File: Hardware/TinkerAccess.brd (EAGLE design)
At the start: 65 x 56.5 mm, 46 parts, among them Q1 500mA/300V, Q2 310mA/60V/1.6Ω, U1 SOIC-8SOIC-8

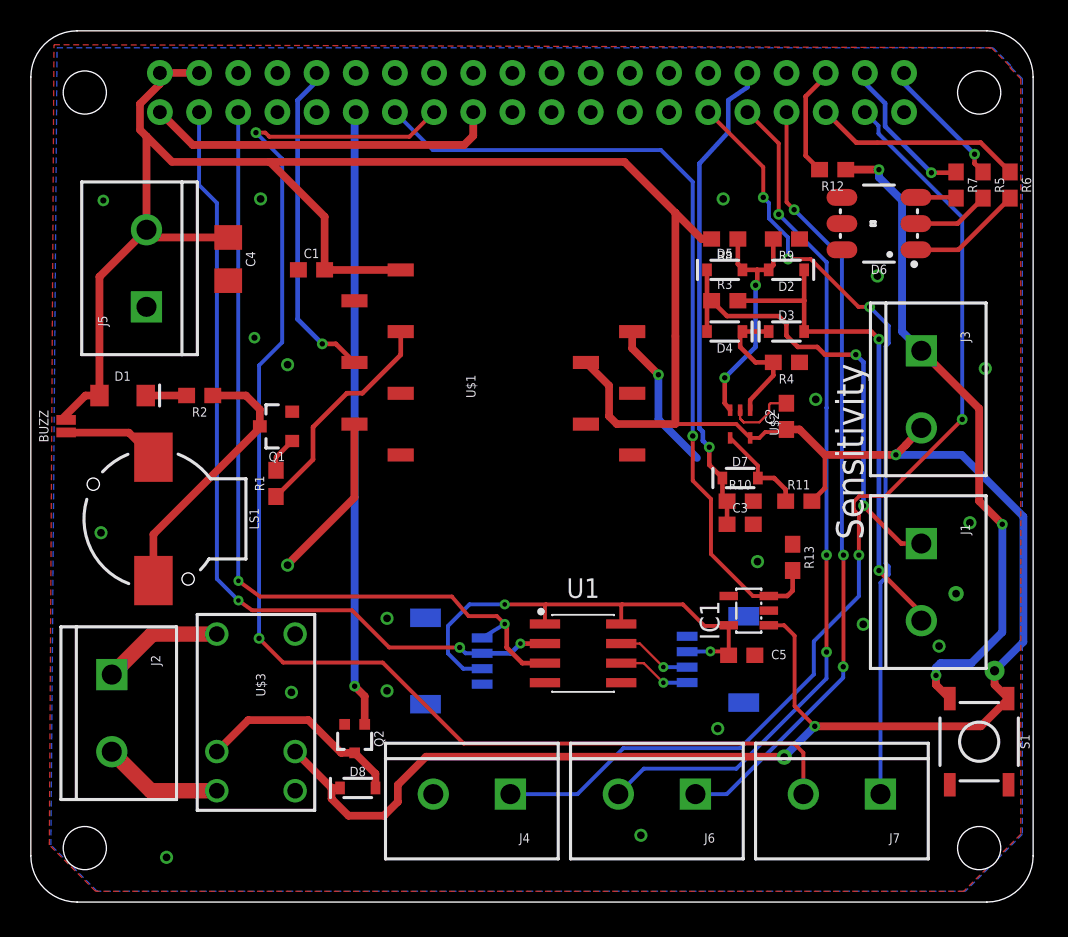
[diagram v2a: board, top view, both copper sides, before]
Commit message: Changes for v1.4 of TinkerAccess PCB
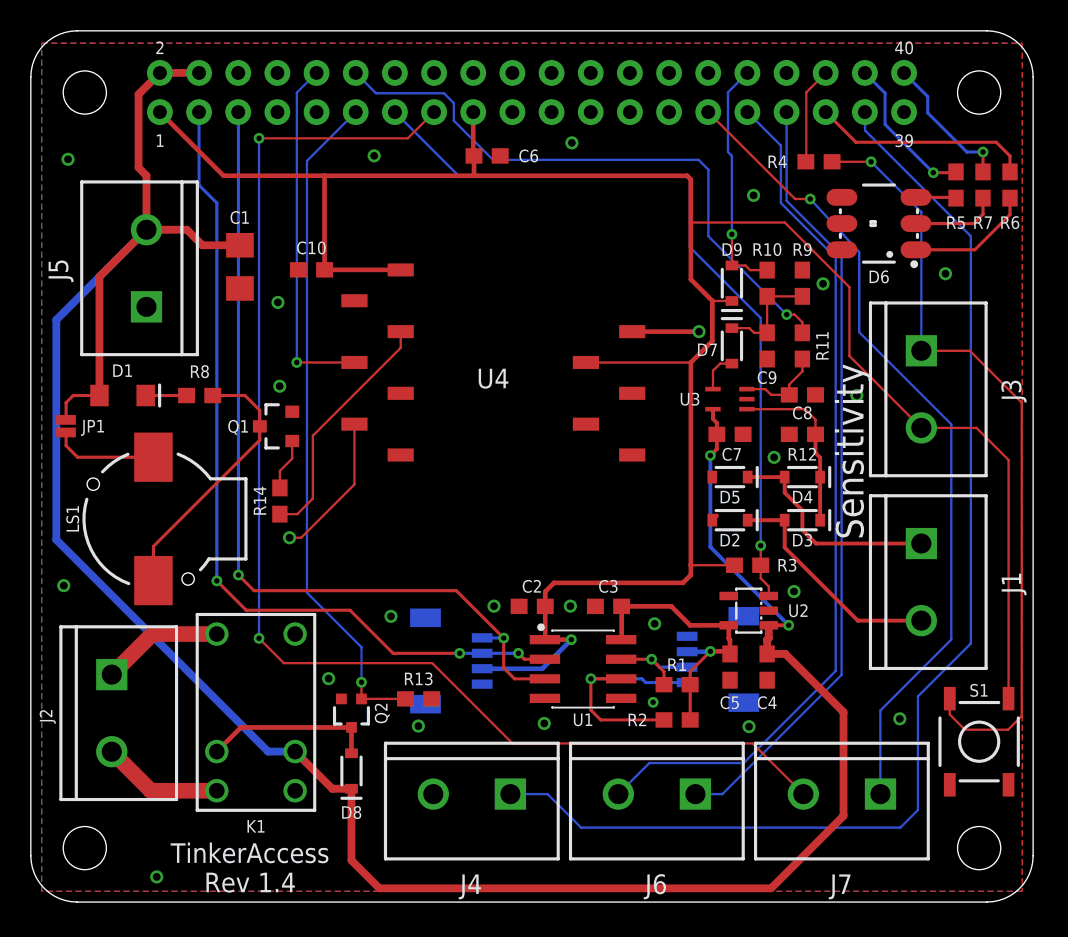
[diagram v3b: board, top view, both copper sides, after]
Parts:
- removed U$2: ADCMP-371, TinkerMill:SC-70-5
- added C10, C7: 0.1uF, SparkFun-Capacitors:0603
- added C6, C8, C9: 1uF, SparkFun-Capacitors:0603
- added D9: 1A/100V, SparkFun-DiscreteSemi:SOD-323
- added LOGO1: MADE_BY_TINKERMILL, TinkerMill:MADE_BY_TINKERMILL
- added R14: 180, SparkFun-Resistors:0603
- added U3: ADCMP-371, TinkerMill:SC-70-5
- C1: value 0.1uF -> 10uF; device SparkFun-Capacitors:0603 -> SparkFun-Capacitors:1206
- C2, C3: value 10uF -> 0.1uF
- C4: value 10uF -> 1uF; device SparkFun-Capacitors:1206 -> SparkFun-Capacitors:0603
- C5: value 10uF -> 1uF
- D2, D3, D4, D5, D7: value 250mA/100V -> 1A/100V
- D8: value 1A/23V/620mV -> 1A/100V
- JP1: value JUMPER-SMT_2_NC_PASTE_NO-SILK -> BUZZ
- LS1: value BUZZER-SMD -> BUZZER
- R1, R2: value 10M -> 10k
- R12: value 10k -> 1k
- R3, R4: value 1k -> 10k
- R5: value 330 -> 300
- R7: value 300 -> 330
- R8: value 1k -> 330
- R9: value 1k -> 100k
- U1: value SOIC-8SOIC-8 -> Si8600AC
- U2: value (none) -> AP2112
- moved C4 43.8 mm to (47.8, 15.2)
- moved R2 37.4 mm to (41.9, 11.8)
- moved R8 35.5 mm to (10.9, 32.9)
- moved R1 29.1 mm to (41.9, 14.1), turned to 180 degrees
- moved R13 25.9 mm to (25.1, 13.2), turned to 0 degrees
- moved C2 20.6 mm to (32.5, 19.2), turned to 0 degrees
- moved R12 17.3 mm to (50.0, 30.3), turned to 0 degrees
- moved R3 17.2 mm to (46.5, 21.8)
- moved D2 16.6 mm to (45.3, 24.8)
- moved R10 14.2 mm to (47.8, 40.1), turned to 90 degrees
- moved D5 13.4 mm to (45.3, 27.6), turned to 180 degrees
- moved R4 13.2 mm to (51.1, 48.0)
- moved D3 12.3 mm to (50.0, 24.8), turned to 180 degrees
- moved D4 10.7 mm to (50.0, 27.6)
- moved R11 10.1 mm to (50.0, 36.1), turned to 270 degrees
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- renumbered BUZZ to JP1, IC1 to U2, U$1 to U4, U$3 to K1
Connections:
- removed net N$8: U1.5
- removed net RECT-: D2.A, D5.A, R8.1, R9.2, U$2.P$3
- new net DETECT: C9.1, D7.C, R10.1, R9.1
- new net VREF: C8.1, R11.2, U3.3
- net +3V3: now also C3.2, R1.1, R2.1; no longer J8.2, U1.1
- net 3.3V: now also C10.2, C2.2, C6.1, D9.C, J3.2, J8.2, R3.1, S1.1, U1.1, U4.11, U4.2
- net 3.3V_EN: now also R3.2; no longer R13.2
- net 5V: now also C1.1, C7.1, U3.5; no longer C1.2, C2.1, J3.2, R11.2, R8.2, S1.1, U$2.P$5, U4.11, U4.2
- net AC1: no longer R3.1
- net AC2: no longer R3.2
- net BSCL: now also R2.2
- net BSDA: now also R1.2
- net COMPOUT: now also U3.4; no longer R11.1, U$2.P$4
- net GND: now also C1.2, C10.1, C2.1, C3.1, C6.2, C7.2, C8.2, C9.2, D2.A, D5.A, R12.1, R13.2, R9.2, U1.5, U3.2; no longer C1.1, C2.2, C3.2, R10.2, R13.1, R4.1, R9.1, U$2.P$2
- net GPIO12: now also D9.A, R10.2; no longer C3.1, D7.C, R10.1
- net GPIO16: now also R4.2; no longer R12.2
- net GPIO18: now also R11.1
- net LED_BLUE: now also R5.1; no longer R7.1
- net LED_RED: now also R7.1; no longer R5.1
- net LED_RFID: now also R14.1; no longer R1.1
- net LOGOUT: now also R4.1; no longer R12.1
- net N$1: now also R14.2; no longer R1.2
- net N$11: now also R5.2; no longer R7.2
- net N$3: now also R8.1; no longer R2.1
- net N$4: now also R8.2; no longer R2.2
- net N$9: now also R7.2; no longer R5.2
- net RECT+: now also R12.2, U3.1; no longer R4.2, U$2.P$1
- net RELAY: now also R13.1
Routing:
- net 3.3V: track 23.0 -> 155.5 mm, vias 0 -> 1
- net 5V: track 215.4 -> 156.5 mm, vias 4 -> 2
- net GPIO18: track 0.00 -> 39.5 mm, vias 0 -> 1
- net AC2: track 32.7 -> 15.0 mm, vias 2 -> 0
- net RECT-: track 16.1 -> 0.00 mm, vias 2 -> 0
- net AC1: track 30.3 -> 14.4 mm, vias 2 -> 0
- net GPIO12: track 31.4 -> 15.5 mm
- net +3V3: track 31.0 -> 19.4 mm, vias 2 -> 1
- net GND: track 25.8 -> 14.3 mm, vias 22 -> 25
- net BSCL: track 4.80 -> 15.4 mm
- net GPIO26: track 67.2 -> 77.3 mm, vias 2 -> 0
- net LOGOUT: track 43.1 -> 50.8 mm, vias 3 -> 1
- net DETECT: track 0.00 -> 7.06 mm
- net VREF: track 0.00 -> 5.58 mm
- net RELAY: track 40.0 -> 43.7 mm
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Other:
- board text added: "1"
- board text added: "2"
- board text added: "39"
- board text added: "40"
- board text added: "TinkerAccess Rev 1.4"
